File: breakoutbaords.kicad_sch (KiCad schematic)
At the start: 10 parts, among them J13 USB_A, J15 Conn_02x16_Row_Letter_Last, J16 Conn_02x12_Row_Letter_Last, U3 AMS1117-3.3

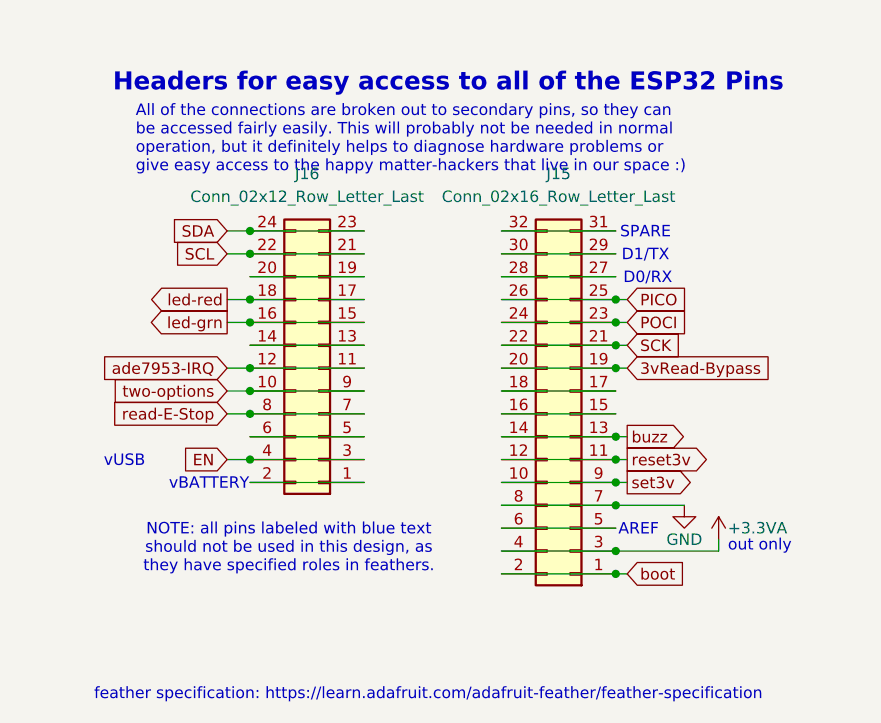
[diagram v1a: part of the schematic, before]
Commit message: unpopulate headers that are not needed
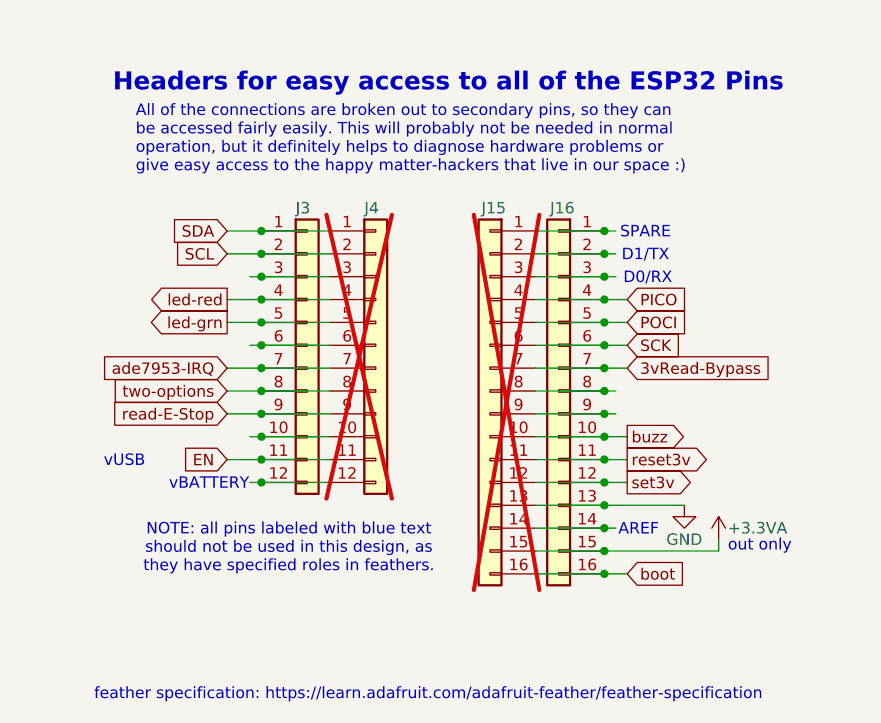
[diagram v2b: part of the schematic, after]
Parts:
- removed J15: Conn_02x16_Row_Letter_Last, Connector_PinHeader_2.54mm:PinHeader_2x16_P2.54mm_Vertical, symbol Connector_Generic:Conn_02x16_Odd_Even
- removed J16: Conn_02x12_Row_Letter_Last, Connector_PinHeader_2.54mm:PinHeader_2x12_P2.54mm_Vertical, symbol Connector_Generic:Conn_02x12_Odd_Even
- added J15, J16: Conn_01x16, Connector_PinSocket_2.54mm:PinSocket_1x16_P2.54mm_Vertical, symbol Connector_Generic:Conn_01x16
- added J3, J4: Conn_01x12, Connector_PinSocket_2.54mm:PinSocket_1x12_P2.54mm_Vertical, symbol Connector_Generic:Conn_01x12
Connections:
- net +3.3VA: now also J15.15 (Pin_15), J16.15 (Pin_15)
- net 3vRead-Bypass: now also J15.7 (Pin_7), J16.7 (Pin_7)
- net EN: now also J3.11 (Pin_11), J4.11 (Pin_11)
- net GND: now also J15.13 (Pin_13), J16.13 (Pin_13)
- net PICO: now also J15.4 (Pin_4), J16.4 (Pin_4)
- net POCI: now also J15.5 (Pin_5), J16.5 (Pin_5)
- net SCK: now also J15.6 (Pin_6), J16.6 (Pin_6)
- net SCL: now also J3.2 (Pin_2), J4.2 (Pin_2)
- net SDA: now also J3.1 (Pin_1), J4.1 (Pin_1)
- net ade7953-IRQ: now also J3.7 (Pin_7), J4.7 (Pin_7)
- net boot: now also J15.16 (Pin_16), J16.16 (Pin_16)
- net buzz: now also J15.10 (Pin_10), J16.10 (Pin_10)
- net led-grn: now also J3.5 (Pin_5), J4.5 (Pin_5)
- net led-red: now also J3.4 (Pin_4), J4.4 (Pin_4)
- net read-E-Stop: now also J3.9 (Pin_9), J4.9 (Pin_9)
- net reset3v: now also J15.11 (Pin_11), J16.11 (Pin_11)
- net set3v: now also J15.12 (Pin_12), J16.12 (Pin_12)
- net two-options: now also J3.8 (Pin_8), J4.8 (Pin_8)
- new net: J3.10 (Pin_10), J4.10 (Pin_10)
- new net: J3.12 (Pin_12), J4.12 (Pin_12)
- new net: J3.3 (Pin_3), J4.3 (Pin_3)
- new net: J3.6 (Pin_6), J4.6 (Pin_6)
- new net: J15.1 (Pin_1), J16.1 (Pin_1)
- new net: J15.14 (Pin_14), J16.14 (Pin_14)
- new net: J15.2 (Pin_2), J16.2 (Pin_2)
- new net: J15.3 (Pin_3), J16.3 (Pin_3)
- new net: J15.8 (Pin_8), J16.8 (Pin_8)
- new net: J15.9 (Pin_9), J16.9 (Pin_9)

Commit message: added candidate changes to accomodate Adafruit Ethernet feather-wing
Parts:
- pwr5v1: now left out of the parts list
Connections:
- net GND: no longer SPI-1.4 (Pin_4)
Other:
- note added: "<-- candidate"
- note added: "https://learn.adafruit.com/ adafruit-wiz5500-wiznet- ethernet-featherwing/pinouts"
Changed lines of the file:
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@@
-	)
-	(junction
-		(at 193.04 90.17)
-		(diameter 0)
-		(color 0 0 0 0)
 	)
 	(junction
@@
 	(wire
 		(pts
-			(xy 193.04 85.09) (xy 193.04 90.17)
-		)
-		(stroke
-			(width 0)
-			(type default)
-		)
-	)
-	(wire
-		(pts
 			(xy 99.06 161.29) (xy 101.6 161.29)
 		)
@@
 	(wire
 		(pts
+			(xy 52.07 151.13) (xy 57.15 151.13)
+		)
+		(stroke
+			(width 0)
+			(type default)
+		)
+	)
+	(wire
+		(pts
 			(xy 73.66 81.28) (xy 73.66 83.82)
 		)
@@
 	(wire
 		(pts
-			(xy 204.47 85.09) (xy 193.04 85.09)
-		)
-		(stroke
-			(width 0)
-			(type default)
-		)
-	)
-	(wire
-		(pts
 			(xy 57.15 156.21) (xy 60.96 156.21)
 		)
@@
 	(wire
 		(pts
+			(xy 191.77 85.09) (xy 201.93 85.09)
+		)
+		(stroke
+			(width 0)
+			(type default)
+		)
+	)
+	(wire
+		(pts
 			(xy 138.43 100.33) (xy 140.97 100.33)
 		)
@@
 		(pts
 			(xy 91.44 148.59) (xy 99.06 148.59)
+		)
+		(stroke
+			(width 0)
+			(type default)
+		)
+	)
+	(wire
+		(pts
+			(xy 101.6 156.21) (xy 106.68 156.21)
 		)
 		(stroke
@@
 		)
 	)
+	(text "https://learn.adafruit.com/\nadafruit-wiz5500-wiznet-\nethernet-featherwing/pinouts"
+		(exclude_from_sim no)
+		(at 26.67 150.876 0)
+		(effects
+			(font
+				(size 1.27 1.27)
+			)
+		)
+	)
 	(text "D0/RX"
 		(exclude_from_sim no)
@@
 			)
 			(href "https://learn.adafruit.com/adafruit-feather/feather-specification")
+		)
+	)
+	(text "<-- candidate"
+		(exclude_from_sim no)
+		(at 123.444 156.464 0)
+		(effects
+			(font
+				(size 1.27 1.27)
+			)
 		)
 	)
@@
 		)
 	)
+	(text "<-- candidate"
+		(exclude_from_sim no)
+		(at 217.424 85.09 0)
+		(effects
+			(font
+				(size 1.27 1.27)
+			)
+		)
+	)
 	(text "There are only enough pins to cinfigure a single \nSPI connection by pulling the 'chip select' to GND\nwith all the other pins needed on the board.\nFor this reason, choose your SPI friends wisely."
 		(exclude_from_sim no)
@@
 		)
 	)
+	(global_label "CS-eth0"
+		(shape output)
+		(at 52.07 151.13 180)
+		(fields_autoplaced yes)
+		(effects
+			(font
+				(size 1.27 1.27)
+			)
+			(justify right)
+		)
+		(property "Intersheetrefs" "${INTERSHEET_REFS}"
+			(at 40.8601 151.13 0)
+			(effects
+				(font
+					(size 1.27 1.27)
+				)
+				(justify right)
+				(hide yes)
+			)
+		)
+	)
 	(global_label "POCI"
 		(shape input)
@@
 		)
 	)
+	(global_label "CS-jst"
+		(shape input)
+		(at 191.77 85.09 180)
+		(fields_autoplaced yes)
+		(effects
+			(font
+				(size 1.27 1.27)
+			)
+			(justify right)
+		)
+		(property "Intersheetrefs" "${INTERSHEET_REFS}"
+			(at 182.3743 85.09 0)
+			(effects
+				(font
+					(size 1.27 1.27)
+				)
+				(justify right)
+				(hide yes)
+			)
+		)
+	)
 	(global_label "SCL"
 		(shape input)
@@
 				)
 				(justify right)
+				(hide yes)
+			)
+		)
+	)
+	(global_label "CS-jst"
+		(shape output)
+		(at 106.68 156.21 0)
+		(fields_autoplaced yes)
+		(effects
+			(font
+				(size 1.27 1.27)
+			)
+			(justify left)
+		)
+		(property "Intersheetrefs" "${INTERSHEET_REFS}"
+			(at 116.0757 156.21 0)
+			(effects
+				(font
+					(size 1.27 1.27)
+				)
+				(justify left)
 				(hide yes)
 			)
@@
 		(unit 1)
 		(exclude_from_sim no)
-		(in_bom yes)
-		(on_board yes)
+		(in_bom no)
+		(on_board no)
 		(dnp no)
 		(fields_autoplaced yes)

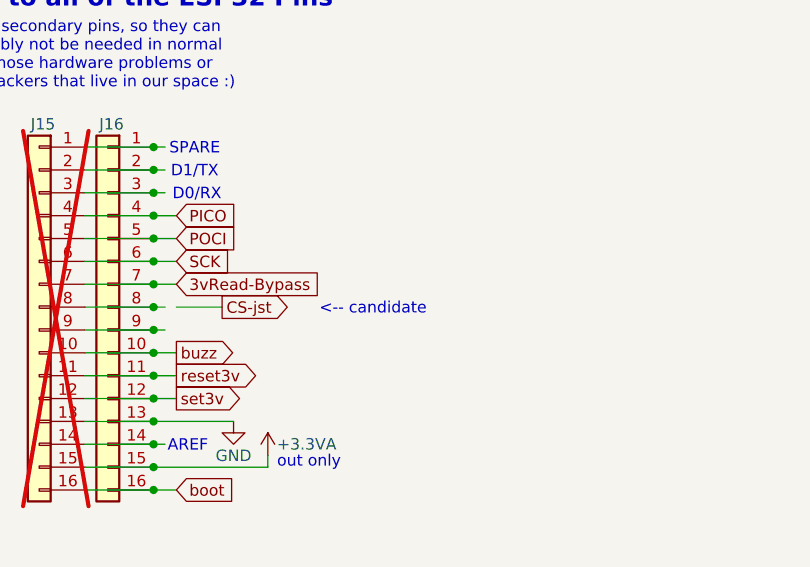
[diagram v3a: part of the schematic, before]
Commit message: reassigned netclasses, removed vestigial level-shifter
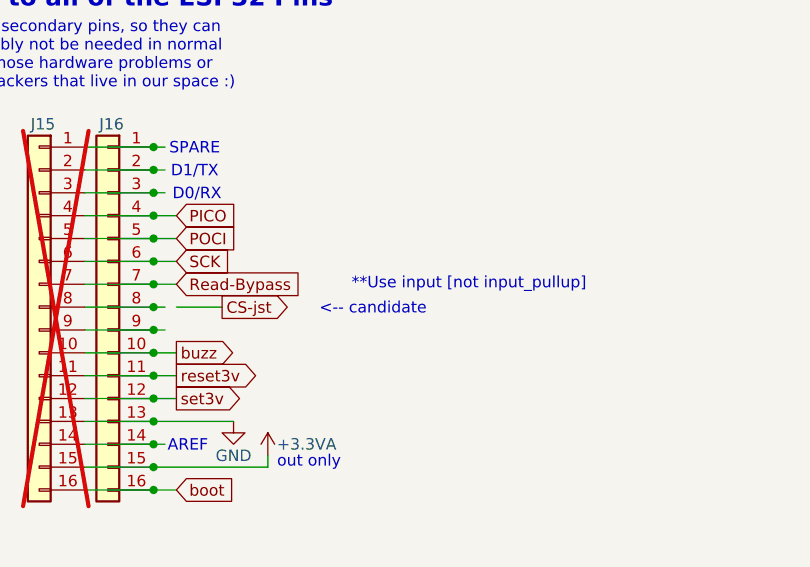
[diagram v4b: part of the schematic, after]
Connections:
- net 3vRead-Bypass renamed Read-Bypass
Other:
- note added: "**Use input [not input_pullup]"
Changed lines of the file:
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@@
+		)
+	)
+	(text "**Use input [not input_pullup]"
+		(exclude_from_sim no)
+		(at 134.112 153.67 0)
+		(effects
+			(font
+				(size 1.27 1.27)
+			)
 		)
 	)
@@
 		)
 	)
-	(global_label "3vRead-Bypass"
+	(global_label "Read-Bypass"
 		(shape input)
 		(at 101.6 153.67 0)
@@
 		)
 		(property "Intersheetrefs" "${INTERSHEET_REFS}"
-			(at 119.5831 153.67 0)
-			(effects
-				(font
+			(at 117.406 153.67 0)
+			(effects
+				(font

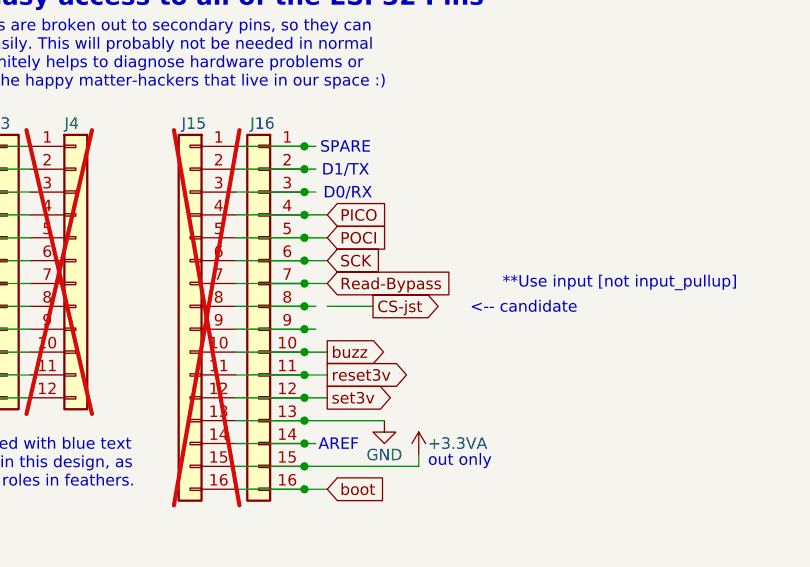
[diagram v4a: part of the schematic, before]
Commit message: [fix] read-bypass link
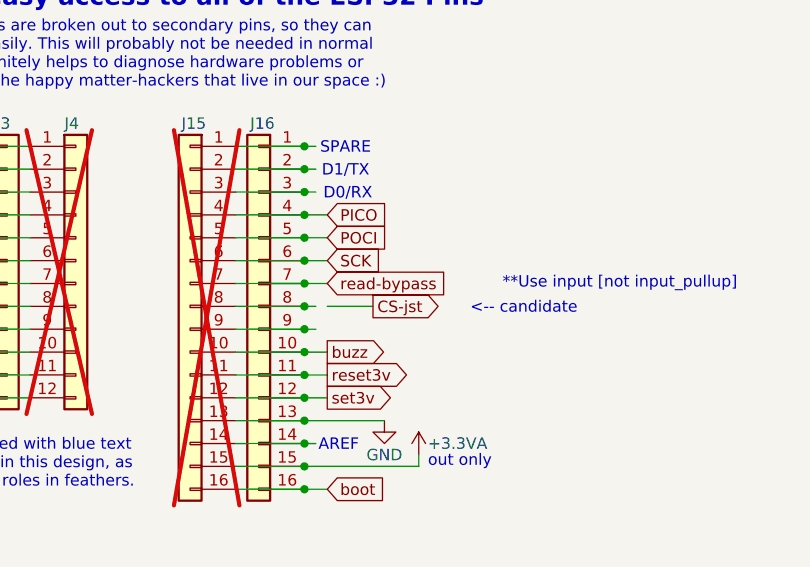
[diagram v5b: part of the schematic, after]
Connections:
- net Read-Bypass renamed read-bypass
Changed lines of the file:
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@@
 		)
 	)
-	(global_label "Read-Bypass"
+	(global_label "read-bypass"
 		(shape input)
 		(at 101.6 153.67 0)
@@
 		)
 		(property "Intersheetrefs" "${INTERSHEET_REFS}"
-			(at 117.406 153.67 0)
+			(at 116.8012 153.67 0)
 			(effects
 				(font

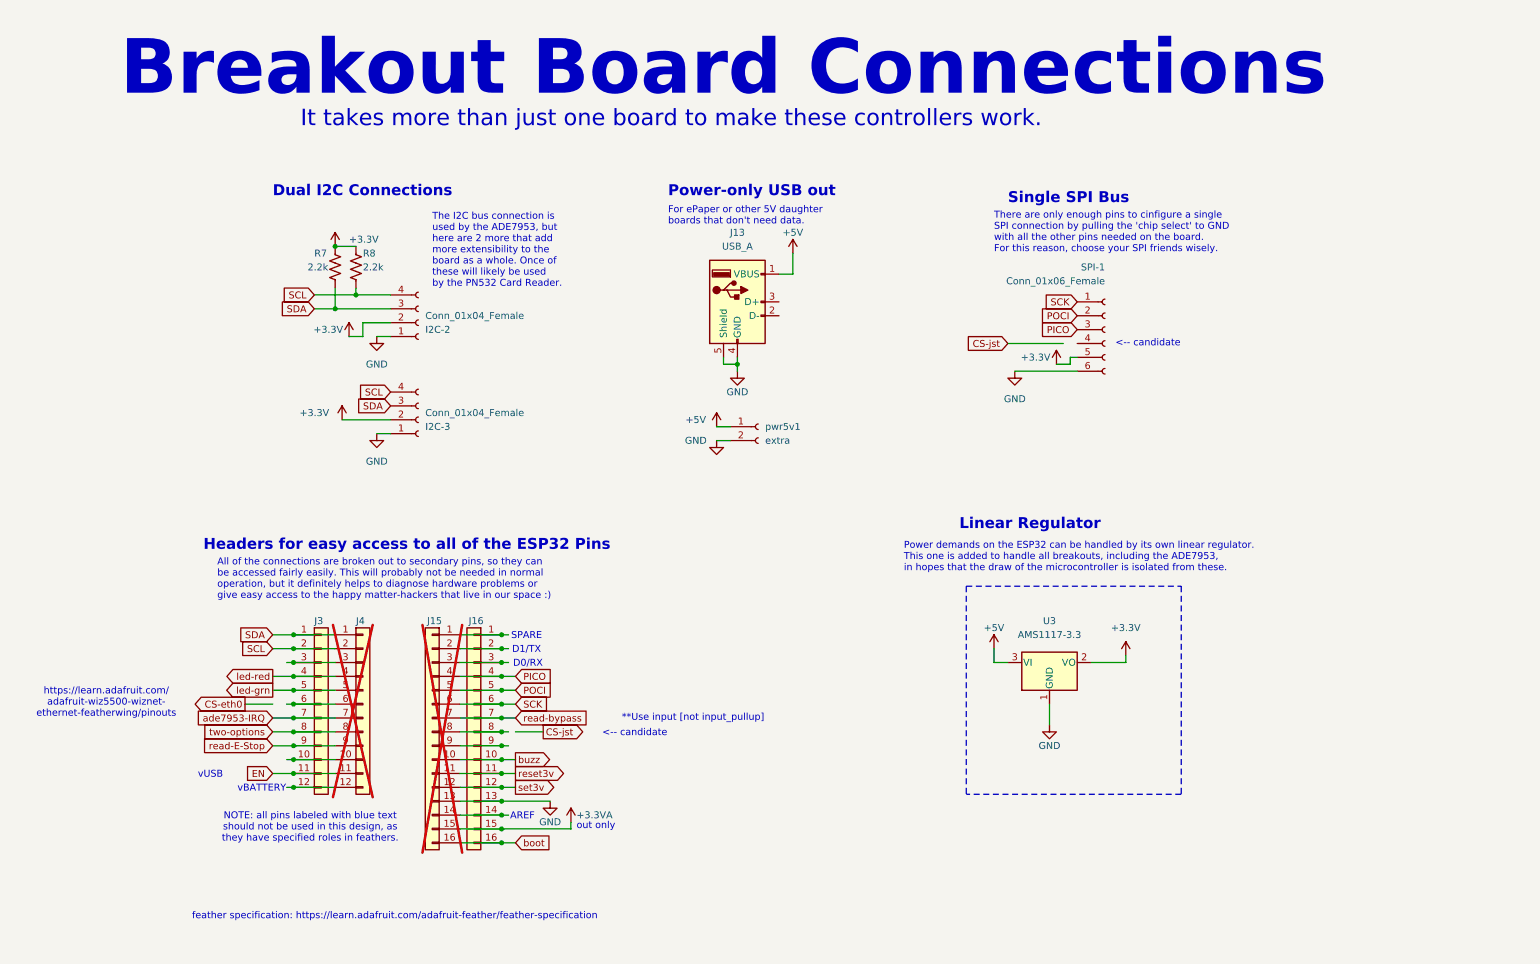
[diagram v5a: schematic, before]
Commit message: [new] assigned CS pin for JST-SPI and Ethernet Feather-Wing
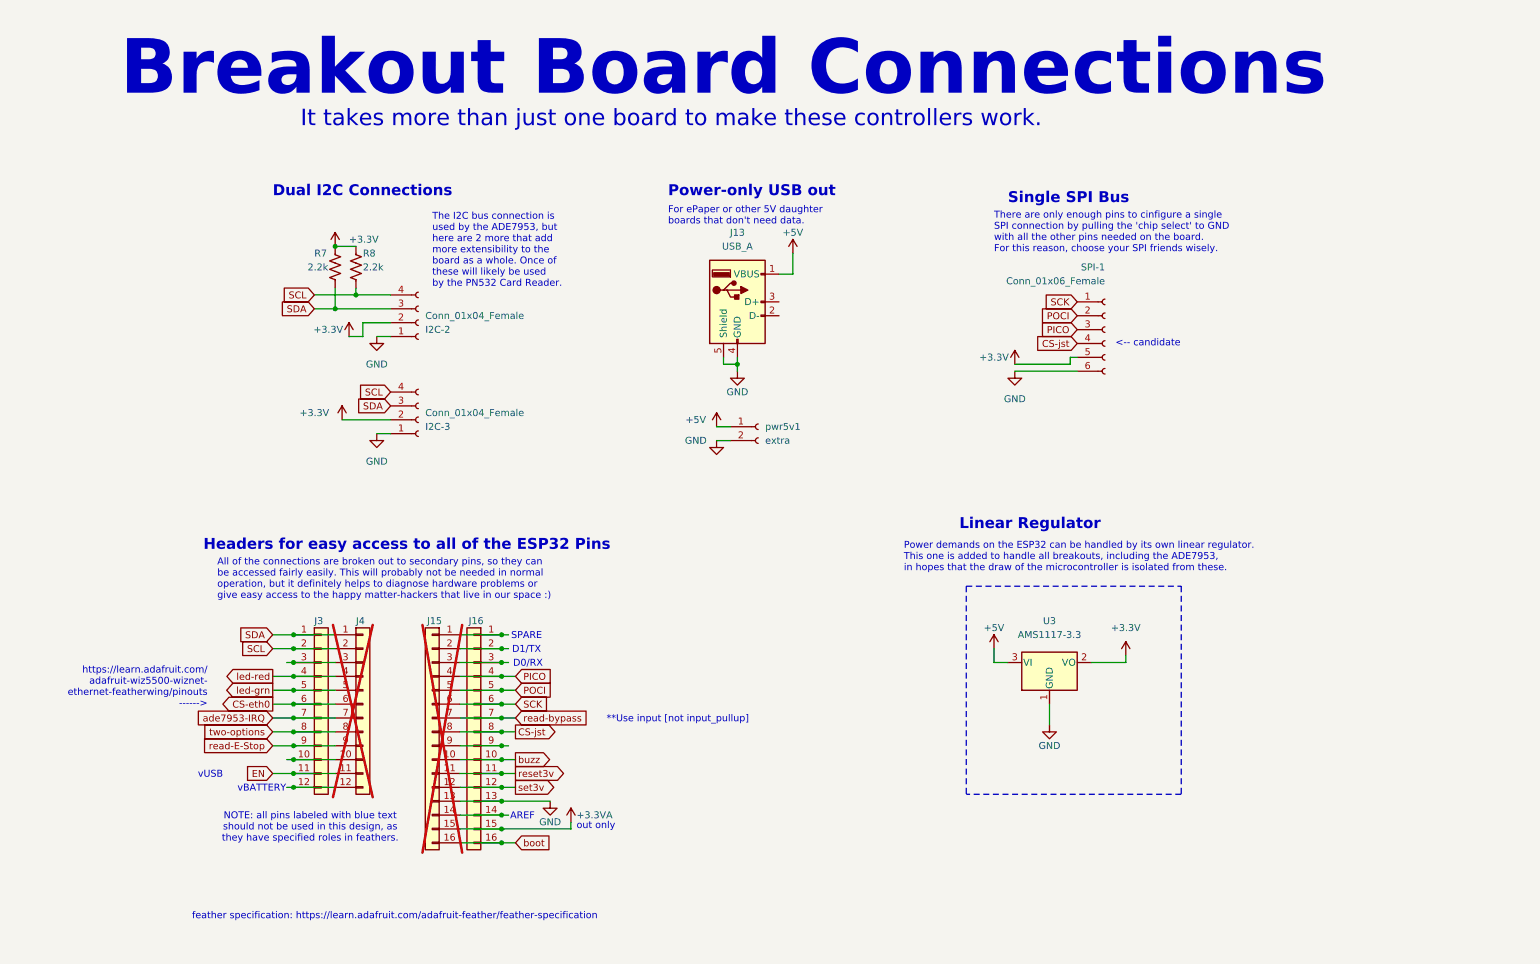
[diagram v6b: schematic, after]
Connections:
- net CS-eth0: now also J3.6 (Pin_6), J4.6 (Pin_6)
- net CS-jst: now also J15.8 (Pin_8), J16.8 (Pin_8), SPI-1.4 (Pin_4)
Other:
- note added: "https://learn.adafruit.com/ adafruit-wiz5500-wiznet- ethernet-featherwing/pinouts ------>"
- note removed: "https://learn.adafruit.com/ adafruit-wiz5500-wiznet- ethernet-featherwing/pinouts"
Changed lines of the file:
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@@
 	(wire
 		(pts
-			(xy 203.2 88.9) (xy 200.66 88.9)
+			(xy 203.2 88.9) (xy 193.04 88.9)
 		)
 		(stroke
@@
 	(wire
 		(pts
-			(xy 52.07 151.13) (xy 57.15 151.13)
+			(xy 57.15 151.13) (xy 60.96 151.13)
 		)
 		(stroke
@@
 	(wire
 		(pts
-			(xy 59.69 151.13) (xy 60.96 151.13)
-		)
-		(stroke
-			(width 0)
-			(type default)
-		)
-	)
-	(wire
-		(pts
 			(xy 60.96 166.37) (xy 68.58 166.37)
 		)
@@
 	(wire
 		(pts
-			(xy 191.77 85.09) (xy 201.93 85.09)
-		)
-		(stroke
-			(width 0)
-			(type default)
-		)
-	)
-	(wire
-		(pts
 			(xy 138.43 100.33) (xy 140.97 100.33)
 		)
@@
 	(wire
 		(pts
-			(xy 99.06 156.21) (xy 100.33 156.21)
+			(xy 99.06 156.21) (xy 101.6 156.21)
 		)
 		(stroke
@@
 		(pts
 			(xy 91.44 148.59) (xy 99.06 148.59)
-		)
-		(stroke
-			(width 0)
-			(type default)
-		)
-	)
-	(wire
-		(pts
-			(xy 101.6 156.21) (xy 106.68 156.21)
 		)
 		(stroke
@@
 	(text "**Use input [not input_pullup]"
 		(exclude_from_sim no)
-		(at 134.112 153.67 0)
+		(at 131.318 153.924 0)
 		(effects
 			(font
@@
 		)
 	)
-	(text "https://learn.adafruit.com/\nadafruit-wiz5500-wiznet-\nethernet-featherwing/pinouts"
-		(exclude_from_sim no)
-		(at 26.67 150.876 0)
-		(effects
-			(font
-				(size 1.27 1.27)
-			)
+	(text "https://learn.adafruit.com/\nadafruit-wiz5500-wiznet-\nethernet-featherwing/pinouts\n------>"
+		(exclude_from_sim no)
+		(at 45.212 148.082 0)
+		(effects
+			(font
+				(size 1.27 1.27)
+			)
+			(justify right)
 		)
 	)
@@
 			)
 			(href "https://learn.adafruit.com/adafruit-feather/feather-specification")
-		)
-	)
-	(text "<-- candidate"
-		(exclude_from_sim no)
-		(at 123.444 156.464 0)
-		(effects
-			(font
-				(size 1.27 1.27)
-			)
 		)
 	)
@@
 	(global_label "CS-eth0"
 		(shape output)
-		(at 52.07 151.13 180)
+		(at 57.15 151.13 180)
 		(fields_autoplaced yes)
 		(effects
@@
 		)
 		(property "Intersheetrefs" "${INTERSHEET_REFS}"
-			(at 40.8601 151.13 0)
+			(at 45.9401 151.13 0)
 			(effects
 				(font
@@
 	(global_label "CS-jst"
 		(shape input)
-		(at 191.77 85.09 180)
+		(at 204.47 85.09 180)
 		(fields_autoplaced yes)
 		(effects
@@
 		)
 		(property "Intersheetrefs" "${INTERSHEET_REFS}"
-			(at 182.3743 85.09 0)
+			(at 195.0743 85.09 0)
 			(effects
 				(font
@@
 	(global_label "CS-jst"
 		(shape output)
-		(at 106.68 156.21 0)
+		(at 101.6 156.21 0)
 		(fields_autoplaced yes)
 		(effects
@@
 		)
 		(property "Intersheetrefs" "${INTERSHEET_REFS}"
-			(at 116.0757 156.21 0)
+			(at 110.9957 156.21 0)
 			(effects
 				(font
@@
 		(lib_name "+3.3V_1")
 		(lib_id "power:+3.3V")
-		(at 200.66 88.9 0)
+		(at 193.04 88.9 0)
 		(unit 1)
 		(exclude_from_sim no)
@@
 		(dnp no)
 		(property "Reference" "#PWR0116"
-			(at 200.66 92.71 0)
+			(at 193.04 92.71 0)
 			(effects
 				(font
@@
 		)
 		(property "Value" "+3.3V"
-			(at 196.85 87.63 0)
+			(at 189.23 87.63 0)
 			(effects
 				(font
@@
 		)
 		(property "Footprint" ""
-			(at 200.66 88.9 0)
+			(at 193.04 88.9 0)
 			(effects
 				(font
@@
 		)
 		(property "Datasheet" ""
-			(at 200.66 88.9 0)
+			(at 193.04 88.9 0)
 			(effects
 				(font
@@
 		)
 		(property "Description" ""
-			(at 200.66 88.9 0)
-			(effects
-				(font
+			(at 193.04 88.9 0)
+			(effects
+				(font
